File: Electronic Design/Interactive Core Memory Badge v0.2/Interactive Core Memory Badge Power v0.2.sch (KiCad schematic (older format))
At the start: 14 parts, among them Q21 MMBT4401LT1G, SW1 SW_SPST, U1 Micro_LiPo_Charger

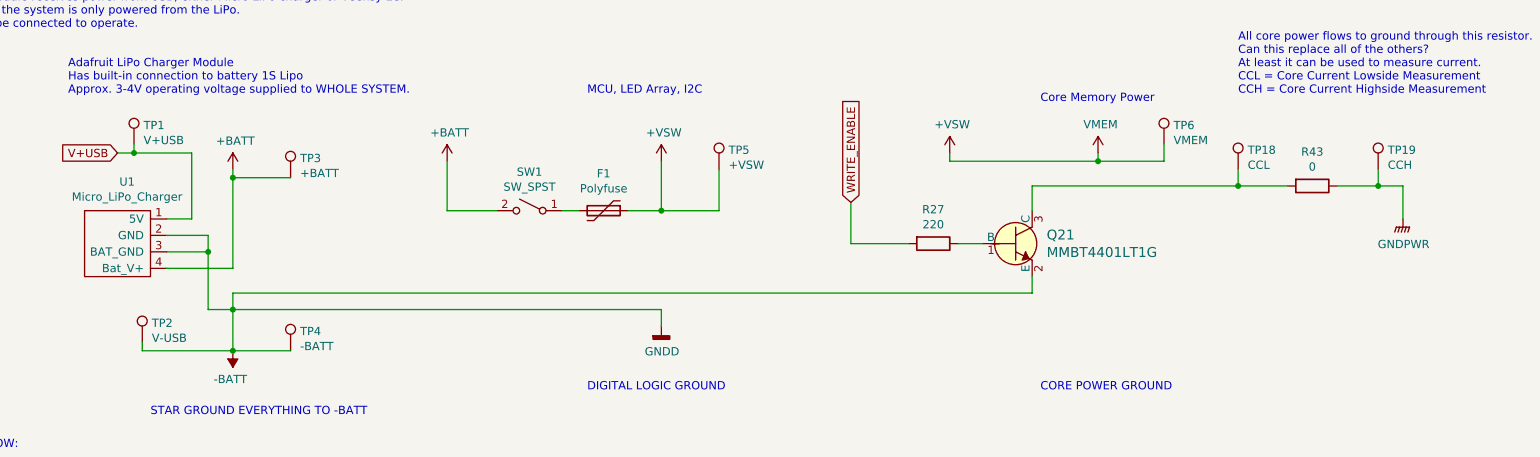
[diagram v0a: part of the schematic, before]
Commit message: Adding discrete OR gate
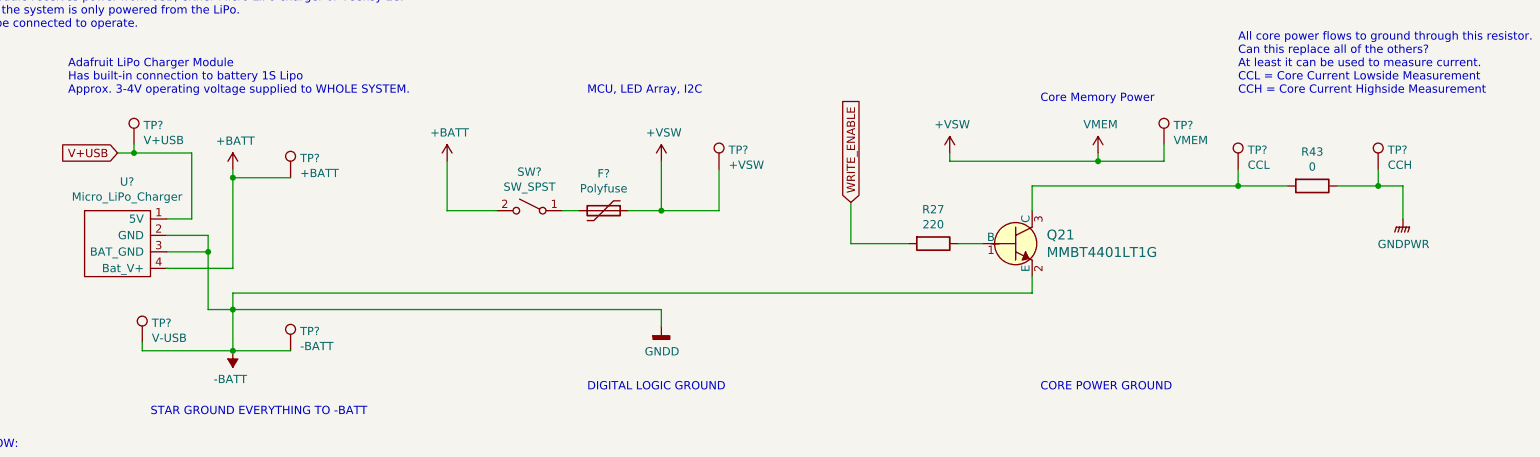
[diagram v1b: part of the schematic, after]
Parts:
- renumbered F1 to F?, SW1 to SW?, TP1 to TP?, TP3 to TP?, TP4 to TP?, TP5 to TP?, TP6 to TP?, TP18 to TP?, TP19 to TP?, TP2 to TP?, U1 to U?
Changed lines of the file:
@@
 EESchema Schematic File Version 4
+LIBS:Interactive Core Memory Badge v0.2-cache
 EELAYER 29 0
 EELAYER END
@@
 $EndDescr
 $Comp
-L power:+BATT #PWR023
+L power:+BATT #PWR?
 U 1 1 5D2956F9
 P 3700 1650
-F 0 "#PWR023" H 3700 1500 50  0001 C CNN
+F 0 "#PWR?" H 3700 1500 50  0001 C CNN
 F 1 "+BATT" H 3715 1823 50  0000 C CNN
 F 2 "" H 3700 1650 50  0001 C CNN
@@
 $EndComp
 $Comp
-L power:VMEM #PWR027
+L power:VMEM #PWR?
 U 1 1 5D2FEB13
 P 7650 1600
-F 0 "#PWR027" H 7650 1450 50  0001 C CNN
+F 0 "#PWR?" H 7650 1450 50  0001 C CNN
 F 1 "VMEM" H 7665 1773 50  0000 C CNN
 F 2 "" H 7650 1600 50  0001 C CNN
@@
 $EndComp
 $Comp
-L Device:Polyfuse F1
+L Device:Polyfuse F?
 U 1 1 5D3009B0
 P 4650 1950
-F 0 "F1" V 4425 1950 50  0000 C CNN
+F 0 "F?" V 4425 1950 50  0000 C CNN
 F 1 "Polyfuse" V 4516 1950 50  0000 C CNN
 F 2 "Fuse:Fuse_0805_2012Metric" H 4700 1750 50  0001 L CNN
@@
 $EndComp
 $Comp
-L Switch:SW_SPST SW1
+L Switch:SW_SPST SW?
 U 1 1 5D30313B
 P 4200 1950
-F 0 "SW1" H 4200 2185 50  0000 C CNN
+F 0 "SW?" H 4200 2185 50  0000 C CNN
 F 1 "SW_SPST" H 4200 2094 50  0000 C CNN
 F 2 "Digikey:Switch_Slide_JS202011SCQN" H 4200 1950 50  0001 C CNN
@@
 	4400 1950 4500 1950
 $Comp
-L power:+VSW #PWR024
+L power:+VSW #PWR?
 U 1 1 5D305A98
 P 5000 1650
-F 0 "#PWR024" H 5000 1500 50  0001 C CNN
+F 0 "#PWR?" H 5000 1500 50  0001 C CNN
 F 1 "+VSW" H 5015 1823 50  0000 C CNN
 F 2 "" H 5000 1650 50  0001 C CNN
@@
 V+USB
 $Comp
-L power:GNDD #PWR025
+L power:GNDD #PWR?
 U 1 1 5D31E05B
 P 5000 2650
-F 0 "#PWR025" H 5000 2400 50  0001 C CNN
+F 0 "#PWR?" H 5000 2400 50  0001 C CNN
 F 1 "GNDD" H 5004 2495 50  0000 C CNN
 F 2 "" H 5000 2650 50  0001 C CNN
@@
 	5000 2550 2400 2550
 $Comp
-L CORE_64_LIBRARY:Micro_LiPo_Charger U1
+L CORE_64_LIBRARY:Micro_LiPo_Charger U?
 U 1 1 5D30894A
 P 1700 2100
-F 0 "U1" H 1758 2425 50  0000 C CNN
+F 0 "U?" H 1758 2425 50  0000 C CNN
 F 1 "Micro_LiPo_Charger" H 1758 2334 50  0000 C CNN
 F 2 "Core_Memory_8x8_Array:Micro_LiPo_Charger" H 1700 2100 50  0001 C CNN
@@
 Connection ~ 2250 2200
 $Comp
-L power:-BATT #PWR022
+L power:-BATT #PWR?
 U 1 1 5D30A5B6
 P 2400 2800
-F 0 "#PWR022" H 2400 2650 50  0001 C CNN
+F 0 "#PWR?" H 2400 2650 50  0001 C CNN
 F 1 "-BATT" H 2415 2973 50  0000 C CNN
 F 2 "" H 2400 2800 50  0001 C CNN
@@
 $EndComp
 $Comp
-L power:+BATT #PWR021
+L power:+BATT #PWR?
 U 1 1 5D30AA43
 P 2400 1700
-F 0 "#PWR021" H 2400 1550 50  0001 C CNN
+F 0 "#PWR?" H 2400 1550 50  0001 C CNN
 F 1 "+BATT" H 2415 1873 50  0000 C CNN
 F 2 "" H 2400 1700 50  0001 C CNN
@@
 	2250 2200 2250 2550
 $Comp
-L power:+VSW #PWR026
+L power:+VSW #PWR?
 U 1 1 5D3925E7
 P 6750 1600
-F 0 "#PWR026" H 6750 1450 50  0001 C CNN
+F 0 "#PWR?" H 6750 1450 50  0001 C CNN
 F 1 "+VSW" H 6765 1773 50  0000 C CNN
 F 2 "" H 6750 1600 50  0001 C CNN
@@
 MCU, LED Array, I2C
 $Comp
-L Connector:TestPoint TP1
+L Connector:TestPoint TP?
 U 1 1 5D48B700
 P 1800 1550
-F 0 "TP1" H 1858 1668 50  0000 L CNN
+F 0 "TP?" H 1858 1668 50  0000 L CNN
 F 1 "V+USB" H 1858 1577 50  0000 L CNN
 F 2 "TestPoint:TestPoint_Keystone_5000-5004_Miniature" H 2000 1550 50  0001 C CNN
@@
 	1800 1600 2150 1600
 $Comp
-L Connector:TestPoint TP3
+L Connector:TestPoint TP?
 U 1 1 5D48C4DD
 P 2750 1750
-F 0 "TP3" H 2808 1868 50  0000 L CNN
+F 0 "TP?" H 2808 1868 50  0000 L CNN
 F 1 "+BATT" H 2808 1777 50  0000 L CNN
 F 2 "TestPoint:TestPoint_Keystone_5000-5004_Miniature" H 2950 1750 50  0001 C CNN
@@
 	2400 1750 2400 1700
 $Comp
-L Connector:TestPoint TP4
+L Connector:TestPoint TP?
 U 1 1 5D48D068
 P 2750 2800
-F 0 "TP4" H 2808 2918 50  0000 L CNN
+F 0 "TP?" H 2808 2918 50  0000 L CNN
 F 1 "-BATT" H 2808 2827 50  0000 L CNN
 F 2 "TestPoint:TestPoint_Keystone_5000-5004_Miniature" H 2950 2800 50  0001 C CNN
@@
 Connection ~ 2400 2800
 $Comp
-L Connector:TestPoint TP5
+L Connector:TestPoint TP?
 U 1 1 5D48E646
 P 5350 1700
-F 0 "TP5" H 5408 1818 50  0000 L CNN
+F 0 "TP?" H 5408 1818 50  0000 L CNN
 F 1 "+VSW" H 5408 1727 50  0000 L CNN
 F 2 "TestPoint:TestPoint_Keystone_5000-5004_Miniature" H 5550 1700 50  0001 C CNN
@@
 Connection ~ 5000 1950
 $Comp
-L Connector:TestPoint TP6
+L Connector:TestPoint TP?
 U 1 1 5D48F2A7
 P 8050 1550
-F 0 "TP6" H 8108 1668 50  0000 L CNN
+F 0 "TP?" H 8108 1668 50  0000 L CNN
 F 1 "VMEM" H 8108 1577 50  0000 L CNN
 F 2 "TestPoint:TestPoint_Keystone_5000-5004_Miniature" H 8250 1550 50  0001 C CNN
@@
 	5000 1650 5000 1950
 $Comp
-L Connector:TestPoint TP2
+L Connector:TestPoint TP?
 U 1 1 5D542466
 P 1850 2750
-F 0 "TP2" H 1908 2868 50  0000 L CNN
+F 0 "TP?" H 1908 2868 50  0000 L CNN
 F 1 "V-USB" H 1908 2777 50  0000 L CNN
 F 2 "TestPoint:TestPoint_Keystone_5000-5004_Miniature" H 2050 2750 50  0001 C CNN
@@
 All core power flows to ground through this resistor.\nCan this replace all of the others?\nAt least it can be used to measure current.\nCCL = Core Current Lowside Measurement\nCCH = Core Current Highside Measurement
 $Comp
-L Connector:TestPoint TP18
+L Connector:TestPoint TP?
 U 1 1 5D4B94F7
 P 8500 1700
-F 0 "TP18" H 8558 1818 50  0000 L CNN
+F 0 "TP?" H 8558 1818 50  0000 L CNN
 F 1 "CCL" H 8558 1727 50  0000 L CNN
 F 2 "TestPoint:TestPoint_Keystone_5000-5004_Miniature" H 8700 1700 50  0001 C CNN
@@
 $EndComp
 $Comp
-L Connector:TestPoint TP19
+L Connector:TestPoint TP?
 U 1 1 5D4B9C69
 P 9350 1700
-F 0 "TP19" H 9408 1818 50  0000 L CNN
+F 0 "TP?" H 9408 1818 50  0000 L CNN
 F 1 "CCH" H 9408 1727 50  0000 L CNN
 F 2 "TestPoint:TestPoint_Keystone_5000-5004_Miniature" H 9550 1700 50  0001 C CNN

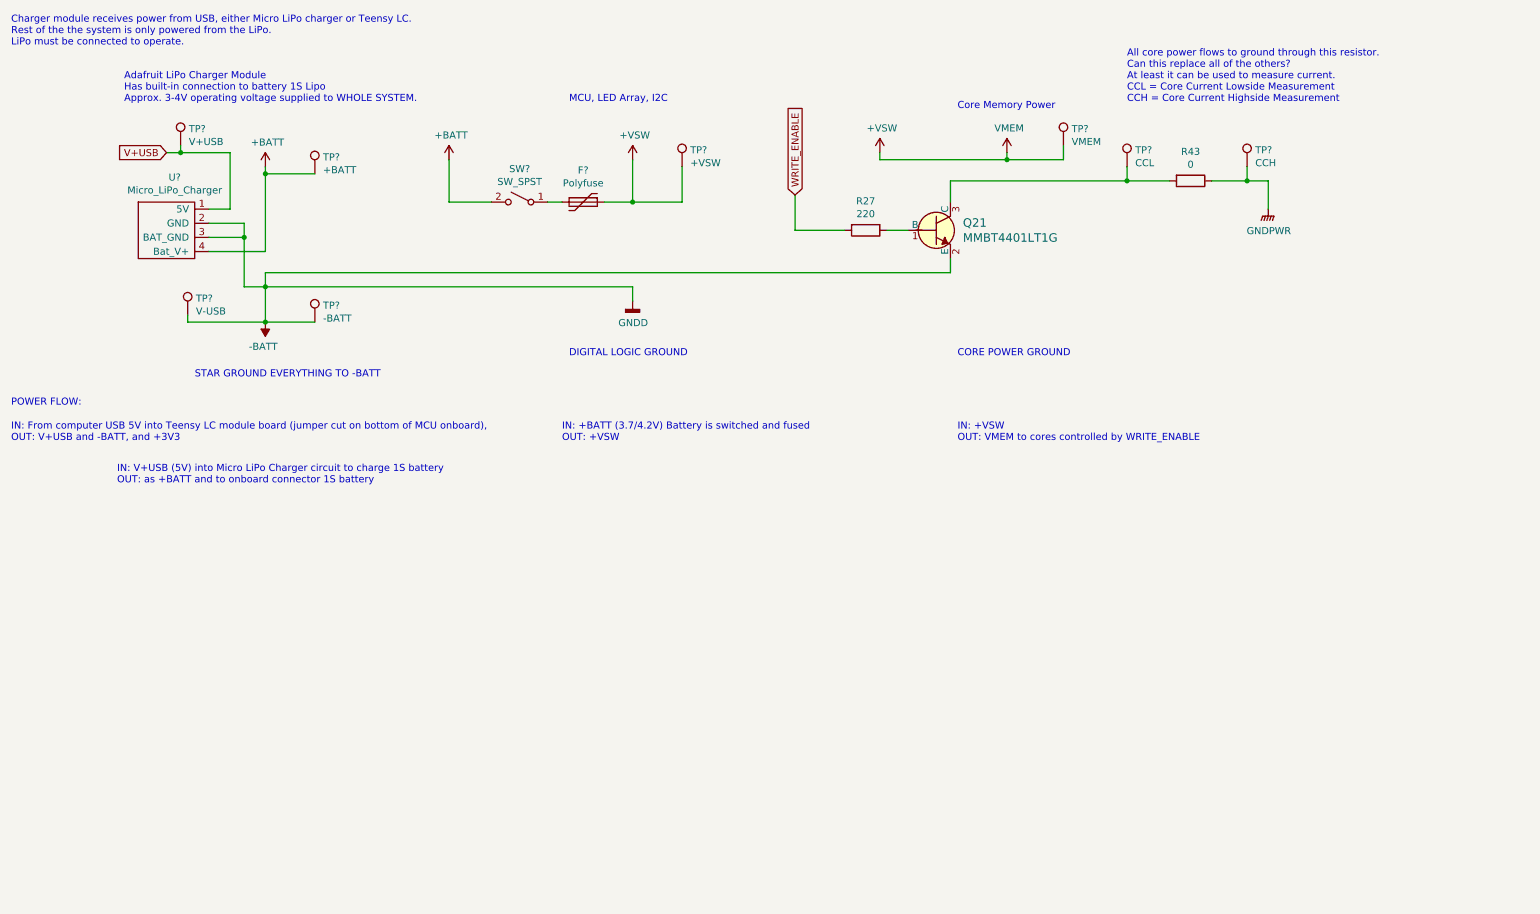
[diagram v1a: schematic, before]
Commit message: Updated drive transistors, switch/diode, OR gate, layout
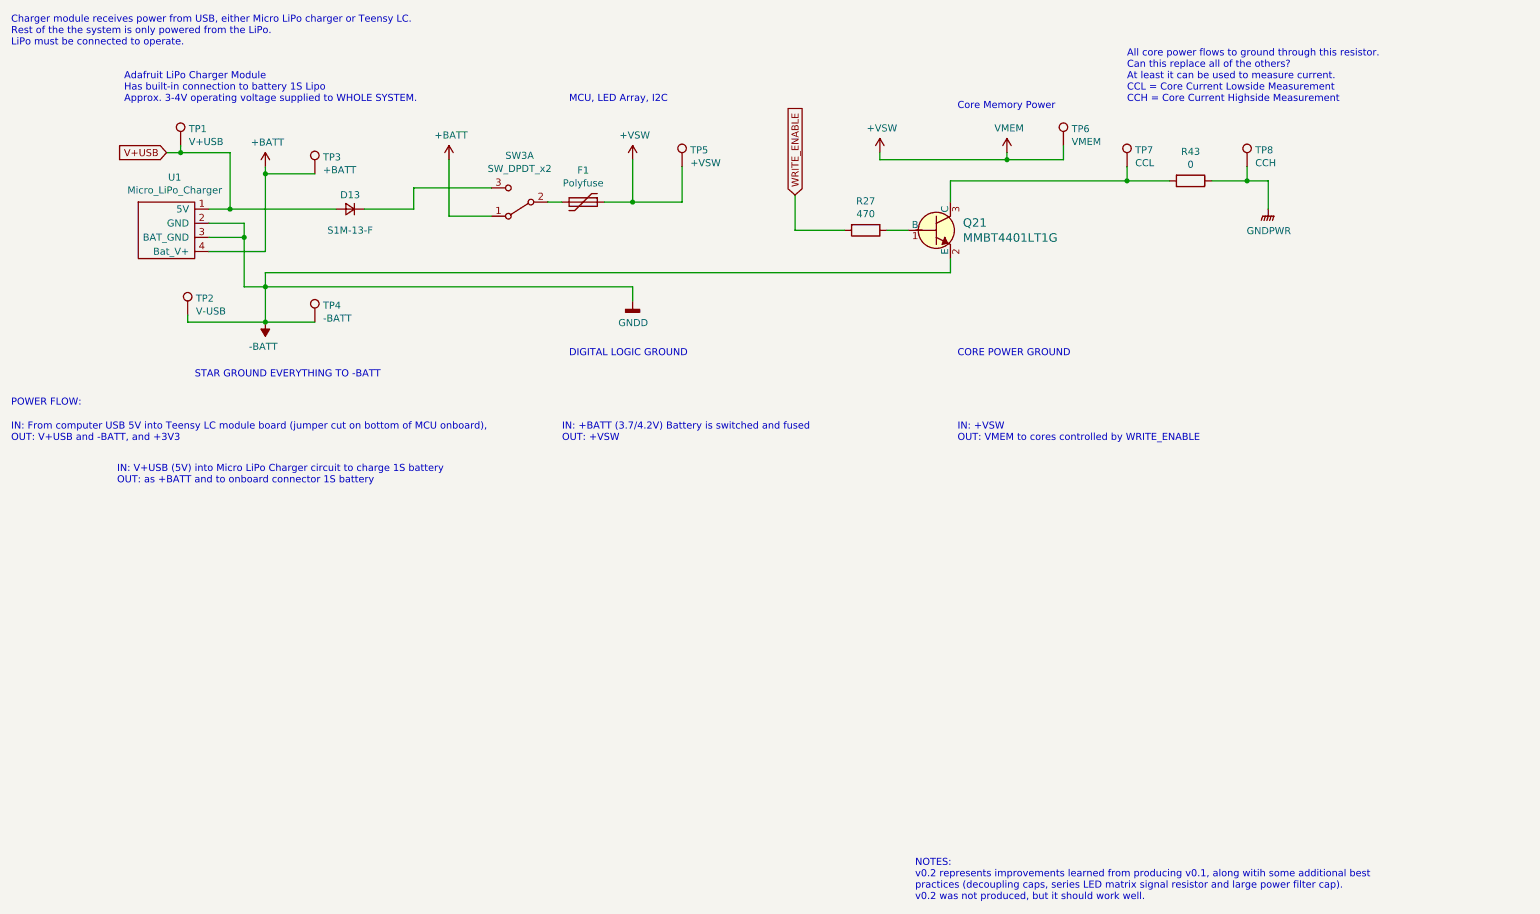
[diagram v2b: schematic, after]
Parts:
- removed SW?: SW_SPST, Digikey:Switch_Slide_JS202011SCQN, symbol Switch:SW_SPST
- added D13: S1M-13-F, Digikey:DO-214AC, symbol Device:D_Small
- added SW3: SW_DPDT_x2, Digikey:Switch_Slide_JS202011SCQN, symbol Switch:SW_DPDT_x2
- R27: value 220 -> 470
- gave numbers to parts that had none: 10
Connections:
- net +BATT: now also SW3.1 (A)
- net V+USB: now also D13.2 (A)
- net at F1.2: now also SW3.2 (B)
- new net: D13.1 (K), SW3.3 (C)
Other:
- note added: "NOTES:\nv0.2 represents improvements learned from producing v0.1, along witih some additional best\npractices (decoupling caps, series LED matrix signal resistor and large power filter cap).\nv0.2 was not produced, but it should work well."
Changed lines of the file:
@@
 encoding utf-8
 Sheet 2 3
-Title ""
-Date ""
-Rev ""
-Comp ""
+Title "Core 64 - Interactive Core Memory Badge"
+Date "2020-03-05"
+Rev "0.2"
+Comp "Andy Geppert - Machine Ideas, LLC"
 Comment1 ""
 Comment2 ""
@@
 $EndDescr
 $Comp
-L power:+BATT #PWR?
+L power:+BATT #PWR023
 U 1 1 5D2956F9
 P 3700 1650
-F 0 "#PWR?" H 3700 1500 50  0001 C CNN
+F 0 "#PWR023" H 3700 1500 50  0001 C CNN
 F 1 "+BATT" H 3715 1823 50  0000 C CNN
 F 2 "" H 3700 1650 50  0001 C CNN
@@
 $EndComp
 $Comp
-L power:VMEM #PWR?
+L power:VMEM #PWR027
 U 1 1 5D2FEB13
 P 7650 1600
-F 0 "#PWR?" H 7650 1450 50  0001 C CNN
+F 0 "#PWR027" H 7650 1450 50  0001 C CNN
 F 1 "VMEM" H 7665 1773 50  0000 C CNN
 F 2 "" H 7650 1600 50  0001 C CNN
@@
 $EndComp
 $Comp
-L Device:Polyfuse F?
+L Device:Polyfuse F1
 U 1 1 5D3009B0
 P 4650 1950
-F 0 "F?" V 4425 1950 50  0000 C CNN
+F 0 "F1" V 4425 1950 50  0000 C CNN
 F 1 "Polyfuse" V 4516 1950 50  0000 C CNN
 F 2 "Fuse:Fuse_0805_2012Metric" H 4700 1750 50  0001 L CNN
@@
 	0    1    1    0
 $EndComp
-$Comp
-L Switch:SW_SPST SW?
-U 1 1 5D30313B
-P 4200 1950
-F 0 "SW?" H 4200 2185 50  0000 C CNN
-F 1 "SW_SPST" H 4200 2094 50  0000 C CNN
-F 2 "Digikey:Switch_Slide_JS202011SCQN" H 4200 1950 50  0001 C CNN
-F 3 "~" H 4200 1950 50  0001 C CNN
-	1    4200 1950
-	-1   0    0    -1
-$EndComp
 Wire Wire Line
 	4400 1950 4500 1950
 $Comp
-L power:+VSW #PWR?
+L power:+VSW #PWR024
 U 1 1 5D305A98
 P 5000 1650
-F 0 "#PWR?" H 5000 1500 50  0001 C CNN
+F 0 "#PWR024" H 5000 1500 50  0001 C CNN
 F 1 "+VSW" H 5015 1823 50  0000 C CNN
 F 2 "" H 5000 1650 50  0001 C CNN
@@
 Adafruit LiPo Charger Module\nHas built-in connection to battery 1S Lipo\nApprox. 3-4V operating voltage supplied to WHOLE SYSTEM.
 Wire Wire Line
-	3700 1950 4000 1950
+	3700 2050 4000 2050
 Wire Wire Line
 	4800 1950 5000 1950
@@
 V+USB
 $Comp
-L power:GNDD #PWR?
+L power:GNDD #PWR025
 U 1 1 5D31E05B
 P 5000 2650
-F 0 "#PWR?" H 5000 2400 50  0001 C CNN
+F 0 "#PWR025" H 5000 2400 50  0001 C CNN
 F 1 "GNDD" H 5004 2495 50  0000 C CNN
 F 2 "" H 5000 2650 50  0001 C CNN
@@
 	5000 2550 2400 2550
 $Comp
-L CORE_64_LIBRARY:Micro_LiPo_Charger U?
+L CORE_64_LIBRARY:Micro_LiPo_Charger U1
 U 1 1 5D30894A
 P 1700 2100
-F 0 "U?" H 1758 2425 50  0000 C CNN
+F 0 "U1" H 1758 2425 50  0000 C CNN
 F 1 "Micro_LiPo_Charger" H 1758 2334 50  0000 C CNN
 F 2 "Core_Memory_8x8_Array:Micro_LiPo_Charger" H 1700 2100 50  0001 C CNN
@@
 Connection ~ 2250 2200
 $Comp
-L power:-BATT #PWR?
+L power:-BATT #PWR022
 U 1 1 5D30A5B6
 P 2400 2800
-F 0 "#PWR?" H 2400 2650 50  0001 C CNN
+F 0 "#PWR022" H 2400 2650 50  0001 C CNN
 F 1 "-BATT" H 2415 2973 50  0000 C CNN
 F 2 "" H 2400 2800 50  0001 C CNN
@@
 $EndComp
 $Comp
-L power:+BATT #PWR?
+L power:+BATT #PWR021
 U 1 1 5D30AA43
 P 2400 1700
-F 0 "#PWR?" H 2400 1550 50  0001 C CNN
+F 0 "#PWR021" H 2400 1550 50  0001 C CNN
 F 1 "+BATT" H 2415 1873 50  0000 C CNN
 F 2 "" H 2400 1700 50  0001 C CNN
@@
 	2250 2200 2250 2550
 $Comp
-L power:+VSW #PWR?
+L power:+VSW #PWR026
 U 1 1 5D3925E7
 P 6750 1600
-F 0 "#PWR?" H 6750 1450 50  0001 C CNN
+F 0 "#PWR026" H 6750 1450 50  0001 C CNN
 F 1 "+VSW" H 6765 1773 50  0000 C CNN
 F 2 "" H 6750 1600 50  0001 C CNN
@@
 AR Path="/5D254AE8/5D35C3CF" Ref="R27"  Part="1"
 F 0 "R27" V 6443 2150 50  0000 C CNN
-F 1 "220" V 6534 2150 50  0000 C CNN
+F 1 "470" V 6534 2150 50  0000 C CNN
 F 2 "Resistor_SMD:R_0805_2012Metric" V 6580 2150 50  0001 C CNN
 F 3 "~" H 6650 2150 50  0001 C CNN
@@
 MCU, LED Array, I2C
 $Comp
-L Connector:TestPoint TP?
+L Connector:TestPoint TP1
 U 1 1 5D48B700
 P 1800 1550
-F 0 "TP?" H 1858 1668 50  0000 L CNN
+F 0 "TP1" H 1858 1668 50  0000 L CNN
 F 1 "V+USB" H 1858 1577 50  0000 L CNN
 F 2 "TestPoint:TestPoint_Keystone_5000-5004_Miniature" H 2000 1550 50  0001 C CNN
@@
 	1800 1600 2150 1600
 $Comp
-L Connector:TestPoint TP?
+L Connector:TestPoint TP3
 U 1 1 5D48C4DD
 P 2750 1750
-F 0 "TP?" H 2808 1868 50  0000 L CNN
+F 0 "TP3" H 2808 1868 50  0000 L CNN
 F 1 "+BATT" H 2808 1777 50  0000 L CNN
 F 2 "TestPoint:TestPoint_Keystone_5000-5004_Miniature" H 2950 1750 50  0001 C CNN
@@
 	2400 1750 2400 1700
 $Comp
-L Connector:TestPoint TP?
+L Connector:TestPoint TP4
 U 1 1 5D48D068
 P 2750 2800
-F 0 "TP?" H 2808 2918 50  0000 L CNN
+F 0 "TP4" H 2808 2918 50  0000 L CNN
 F 1 "-BATT" H 2808 2827 50  0000 L CNN
 F 2 "TestPoint:TestPoint_Keystone_5000-5004_Miniature" H 2950 2800 50  0001 C CNN
@@
 Connection ~ 2400 2800
 $Comp
-L Connector:TestPoint TP?
+L Connector:TestPoint TP5
 U 1 1 5D48E646
 P 5350 1700
-F 0 "TP?" H 5408 1818 50  0000 L CNN
+F 0 "TP5" H 5408 1818 50  0000 L CNN
 F 1 "+VSW" H 5408 1727 50  0000 L CNN
 F 2 "TestPoint:TestPoint_Keystone_5000-5004_Miniature" H 5550 1700 50  0001 C CNN
@@
 Connection ~ 5000 1950
 $Comp
-L Connector:TestPoint TP?
+L Connector:TestPoint TP6
 U 1 1 5D48F2A7
 P 8050 1550
-F 0 "TP?" H 8108 1668 50  0000 L CNN
+F 0 "TP6" H 8108 1668 50  0000 L CNN
 F 1 "VMEM" H 8108 1577 50  0000 L CNN
 F 2 "TestPoint:TestPoint_Keystone_5000-5004_Miniature" H 8250 1550 50  0001 C CNN
@@
 	9500 2000 9500 1800
 Wire Wire Line
-	3700 1950 3700 1650
+	3700 2050 3700 1650
 Wire Wire Line
 	5000 1650 5000 1950
 $Comp
-L Connector:TestPoint TP?
+L Connector:TestPoint TP2
 U 1 1 5D542466
 P 1850 2750
-F 0 "TP?" H 1908 2868 50  0000 L CNN
+F 0 "TP2" H 1908 2868 50  0000 L CNN
 F 1 "V-USB" H 1908 2777 50  0000 L CNN
 F 2 "TestPoint:TestPoint_Keystone_5000-5004_Miniature" H 2050 2750 50  0001 C CNN
@@
 All core power flows to ground through this resistor.\nCan this replace all of the others?\nAt least it can be used to measure current.\nCCL = Core Current Lowside Measurement\nCCH = Core Current Highside Measurement
 $Comp
-L Connector:TestPoint TP?
+L Connector:TestPoint TP7
 U 1 1 5D4B94F7
 P 8500 1700
-F 0 "TP?" H 8558 1818 50  0000 L CNN
+F 0 "TP7" H 8558 1818 50  0000 L CNN
 F 1 "CCL" H 8558 1727 50  0000 L CNN
 F 2 "TestPoint:TestPoint_Keystone_5000-5004_Miniature" H 8700 1700 50  0001 C CNN
@@
 $EndComp
 $Comp
-L Connector:TestPoint TP?
+L Connector:TestPoint TP8
 U 1 1 5D4B9C69
 P 9350 1700
-F 0 "TP?" H 9408 1818 50  0000 L CNN
+F 0 "TP8" H 9408 1818 50  0000 L CNN
 F 1 "CCH" H 9408 1727 50  0000 L CNN
 F 2 "TestPoint:TestPoint_Keystone_5000-5004_Miniature" H 9550 1700 50  0001 C CNN
@@
 Wire Wire Line
 	8500 1800 8800 1800
+Text Notes 7000 6900 0    50   ~ 0
+NOTES:\nv0.2 represents improvements learned from producing v0.1, along witih some additional best\npractices (decoupling caps, series LED matrix signal resistor and large power filter cap).\nv0.2 was not produced, but it should work well.
+$Comp
+L Switch:SW_DPDT_x2 SW3
+U 1 1 5E9AF194
+P 4200 1950
+F 0 "SW3" H 4200 1621 50  0000 C CNN
+F 1 "SW_DPDT_x2" H 4200 1714 50  0000 C CNN
+F 2 "Digikey:Switch_Slide_JS202011SCQN" H 4200 1950 50  0001 C CNN
+F 3 "~" H 4200 1950 50  0001 C CNN
+	1    4200 1950
+	-1   0    0    1
+$EndComp
+Wire Wire Line
+	3450 2000 3450 1850
+Wire Wire Line
+	3450 1850 4000 1850
+$Comp
+L Device:D_Small D13
+U 1 1 5E9B647B
+P 3000 2000
+F 0 "D13" H 3000 1900 50  0000 C CNN
+F 1 "S1M-13-F" H 3000 2150 50  0000 C CNN
+F 2 "Digikey:DO-214AC" H 3000 2000 50  0001 C CNN
+F 3 "~" H 3000 2000 50  0001 C CNN
+	1    3000 2000
+	-1   0    0    1
+$EndComp
+Wire Wire Line
+	3100 2000 3450 2000
+Wire Wire Line
+	2900 2000 2150 2000
+Connection ~ 2150 2000
 $EndSCHEMATC
